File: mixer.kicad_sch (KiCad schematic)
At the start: 22 parts, among them U18 RFFC5072

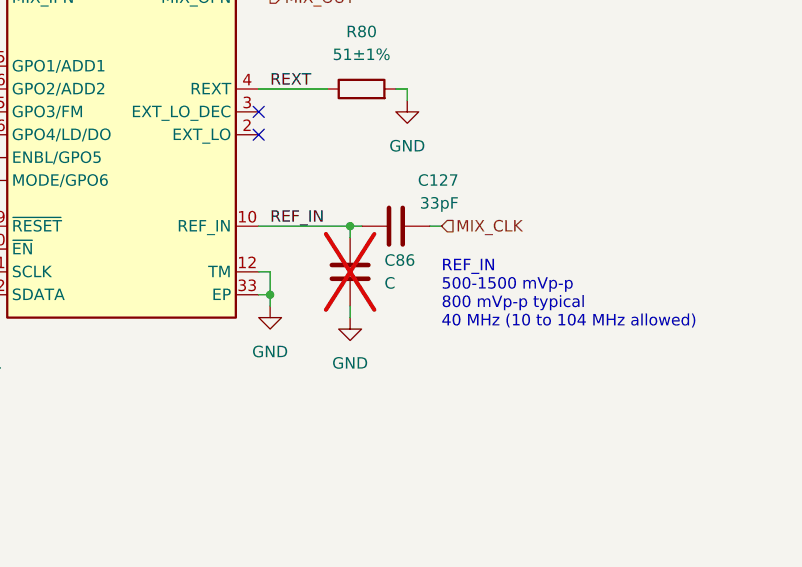
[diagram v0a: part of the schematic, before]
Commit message: update symbol metadata
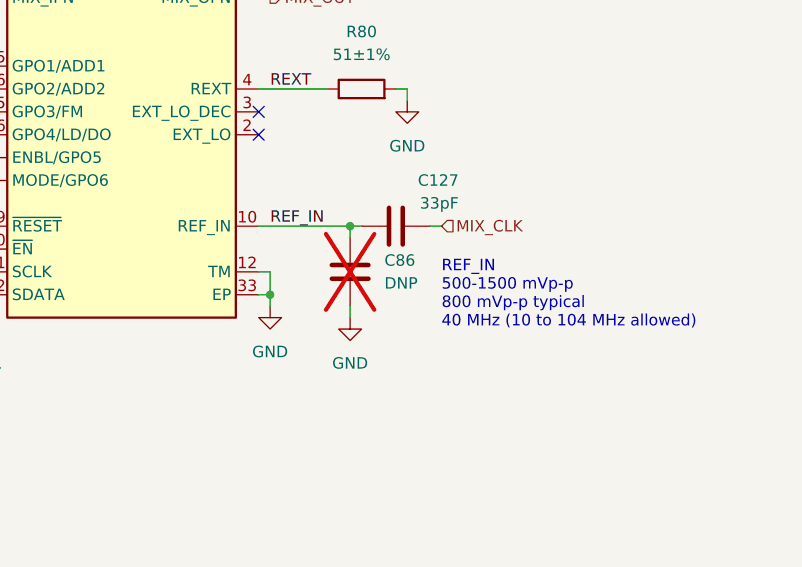
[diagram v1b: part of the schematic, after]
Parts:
- C86: value C -> DNP
- U18: Manufacturer (none) -> Qorvo; Part Number (none) -> RFFC5072TR13; Substitution (none) -> RFFC5072*
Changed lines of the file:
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@@
+      (effects (font (size 1.27 1.27)) hide)
+    )
+    (property "Manufacturer" "Qorvo" (at 156.21 97.79 0)
+      (effects (font (size 1.27 1.27)) hide)
+    )
+    (property "Description" "WIDEBAND SYNTHESIZER/VCO WITH INTEGRATED 6GHz MIXER" (at 156.21 97.79 0)
+      (effects (font (size 1.27 1.27)) hide)
+    )
+    (property "Part Number" "RFFC5072TR13" (at 156.21 97.79 0)
+      (effects (font (size 1.27 1.27)) hide)
+    )
+    (property "Substitution" "RFFC5072*" (at 156.21 97.79 0)
       (effects (font (size 1.27 1.27)) hide)
     )
@@
       (effects (font (size 1.27 1.27)) (justify left))
     )
-    (property "Value" "C" (at 185.42 119.38 0)
-      (effects (font (size 1.27 1.27)) (justify left))
-    )
+    (property "Value" "DNP" (at 185.42 119.38 0)
+      (effects (font (size 1.27 1.27)) (justify left))
+    )

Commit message: Add footprints
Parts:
- C124, C125, C86: footprint (none) -> Capacitor_SMD:C_0201_0603Metric
- R80, R83, R84, R85: footprint (none) -> Resistor_SMD:R_0201_0603Metric
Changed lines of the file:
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@@
       (effects (font (size 1.27 1.27)) (justify left))
     )
-    (property "Footprint" "" (at 216.8652 68.58 0)
+    (property "Footprint" "Capacitor_SMD:C_0201_0603Metric" (at 216.8652 68.58 0)
       (effects (font (size 1.27 1.27)) hide)
     )
@@
       (effects (font (size 1.27 1.27)) (justify left))
     )
-    (property "Footprint" "" (at 209.2452 68.58 0)
+    (property "Footprint" "Capacitor_SMD:C_0201_0603Metric" (at 209.2452 68.58 0)
       (effects (font (size 1.27 1.27)) hide)
     )
@@
       (effects (font (size 1.27 1.27)))
     )
-    (property "Footprint" "" (at 182.88 99.568 90)
+    (property "Footprint" "Resistor_SMD:R_0201_0603Metric" (at 182.88 99.568 90)
       (effects (font (size 1.27 1.27)) hide)
     )
@@
       (effects (font (size 1.27 1.27)))
     )
-    (property "Footprint" "" (at 189.23 61.468 90)
+    (property "Footprint" "Resistor_SMD:R_0201_0603Metric" (at 189.23 61.468 90)
       (effects (font (size 1.27 1.27)) hide)
     )
@@
       (effects (font (size 1.27 1.27)))
     )
-    (property "Footprint" "" (at 199.39 61.468 90)
+    (property "Footprint" "Resistor_SMD:R_0201_0603Metric" (at 199.39 61.468 90)
       (effects (font (size 1.27 1.27)) hide)
     )
@@
       (effects (font (size 1.27 1.27)) (justify right))
     )
-    (property "Footprint" "" (at 217.678 74.93 90)
+    (property "Footprint" "Resistor_SMD:R_0201_0603Metric" (at 217.678 74.93 90)
       (effects (font (size 1.27 1.27)) hide)
     )
@@
       (effects (font (size 1.27 1.27)) (justify left))
     )
-    (property "Footprint" "" (at 182.5752 121.92 0)
-      (effects (font (size 1.27 1.27)) hide)
-    )
+    (property "Footprint" "Capacitor_SMD:C_0201_0603Metric" (at 182.5752 121.92 0)
+      (effects (font (size 1.27 1.27)) hide)
+    )

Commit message: layout wip
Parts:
- C6: footprint Capacitor_SMD:C_0402_1005Metric -> Capacitor_SMD:C_0201_0603Metric; Manufacturer Samsung -> Murata; Part Number CL05C331JB5NNNC -> GRM0335C1E331JA01D; Substitution any equivalent -> GRM0335C1E331JA01*
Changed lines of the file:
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@@
       (effects (font (size 1.27 1.27)) (justify left))
     )
-    (property "Footprint" "Capacitor_SMD:C_0402_1005Metric" (at 185.1152 68.58 0)
+    (property "Footprint" "Capacitor_SMD:C_0201_0603Metric" (at 185.1152 68.58 0)
       (effects (font (size 1.27 1.27)) hide)
     )
@@
       (effects (font (size 1.27 1.27)) hide)
     )
-    (property "Part Number" "CL05C331JB5NNNC" (at 184.15 64.77 0)
-      (effects (font (size 1.27 1.27)) hide)
-    )
-    (property "Substitution" "any equivalent" (at 184.15 64.77 0)
-      (effects (font (size 1.27 1.27)) hide)
-    )
-    (property "Description" "CAP CER 330PF 50V C0G/NP0 0402" (at 184.15 64.77 0)
-      (effects (font (size 1.27 1.27)) hide)
-    )
-    (property "Manufacturer" "Samsung" (at 184.15 64.77 0)
+    (property "Part Number" "GRM0335C1E331JA01D" (at 184.15 64.77 0)
+      (effects (font (size 1.27 1.27)) hide)
+    )
+    (property "Substitution" "GRM0335C1E331JA01*" (at 184.15 64.77 0)
+      (effects (font (size 1.27 1.27)) hide)
+    )
+    (property "Description" "CAP CER 330PF 25V C0G/NP0 0201" (at 184.15 64.77 0)
+      (effects (font (size 1.27 1.27)) hide)
+    )
+    (property "Manufacturer" "Murata" (at 184.15 64.77 0)
       (effects (font (size 1.27 1.27)) hide)
     )
@@
       (effects (font (size 1.27 1.27)) (justify left))
     )
-    (property "Footprint" "Capacitor_SMD:C_0402_1005Metric" (at 195.2752 68.58 0)
+    (property "Footprint" "Capacitor_SMD:C_0201_0603Metric" (at 195.2752 68.58 0)
       (effects (font (size 1.27 1.27)) hide)
     )
@@
       (effects (font (size 1.27 1.27)) hide)
     )
-    (property "Part Number" "CL05C331JB5NNNC" (at 194.31 64.77 0)
-      (effects (font (size 1.27 1.27)) hide)
-    )
-    (property "Substitution" "any equivalent" (at 194.31 64.77 0)
-      (effects (font (size 1.27 1.27)) hide)
-    )
-    (property "Description" "CAP CER 330PF 50V C0G/NP0 0402" (at 194.31 64.77 0)
-      (effects (font (size 1.27 1.27)) hide)
-    )
-    (property "Manufacturer" "Samsung" (at 194.31 64.77 0)
-      (effects (font (size 1.27 1.27)) hide)
-    )
+    (property "Part Number" "GRM0335C1E331JA01D" (at 194.31 64.77 0)
+      (effects (font (size 1.27 1.27)) hide)
+    )
+    (property "Substitution" "GRM0335C1E331JA01*" (at 194.31 64.77 0)
+      (effects (font (size 1.27 1.27)) hide)
+    )
+    (property "Description" "CAP CER 330PF 25V C0G/NP0 0201" (at 194.31 64.77 0)
+      (effects (font (size 1.27 1.27)) hide)
+    )
+    (property "Manufacturer" "Murata" (at 194.31 64.77 0)
+      (effects (font (size 1.27 1.27)) hide)
+    )

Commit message: passive component selections
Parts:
- C124: Manufacturer (none) -> Murata; Part Number (none) -> GRM0335C1H8R2BA01D; Substitution (none) -> GRM0335C1H8R2BA01*
- C125: Manufacturer (none) -> Murata; Part Number (none) -> GRM0335C1H181JA01D; Substitution (none) -> GRM0335C1H181JA01*
- R80: Manufacturer (none) -> Yageo; Part Number (none) -> RC0201FR-0751KL; Substitution (none) -> any equivalent
- R83, R84: Manufacturer (none) -> Yageo; Part Number (none) -> RC0201JR-07470RL; Substitution (none) -> any equivalent
- R85: Manufacturer (none) -> Yageo; Part Number (none) -> RC0201JR-0722KL; Substitution (none) -> any equivalent
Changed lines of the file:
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@@
+      (effects (font (size 1.27 1.27)) hide)
+    )
+    (property "Description" "CAP CER 180PF 50V C0G/NP0 0201" (at 215.9 64.77 0)
+      (effects (font (size 1.27 1.27)) hide)
+    )
+    (property "Manufacturer" "Murata" (at 215.9 64.77 0)
+      (effects (font (size 1.27 1.27)) hide)
+    )
+    (property "Part Number" "GRM0335C1H181JA01D" (at 215.9 64.77 0)
+      (effects (font (size 1.27 1.27)) hide)
+    )
+    (property "Substitution" "GRM0335C1H181JA01*" (at 215.9 64.77 0)
       (effects (font (size 1.27 1.27)) hide)
     )
@@
       (effects (font (size 1.27 1.27)) hide)
     )
+    (property "Description" "CAP CER 8.2PF 50V C0G/NP0 0201" (at 208.28 64.77 0)
+      (effects (font (size 1.27 1.27)) hide)
+    )
+    (property "Manufacturer" "Murata" (at 208.28 64.77 0)
+      (effects (font (size 1.27 1.27)) hide)
+    )
+    (property "Part Number" "GRM0335C1H8R2BA01D" (at 208.28 64.77 0)
+      (effects (font (size 1.27 1.27)) hide)
+    )
+    (property "Substitution" "GRM0335C1H8R2BA01*" (at 208.28 64.77 0)
+      (effects (font (size 1.27 1.27)) hide)
+    )
     (pin "2")
     (pin "1")
@@
     )
     (property "Datasheet" "~" (at 182.88 97.79 0)
+      (effects (font (size 1.27 1.27)) hide)
+    )
+    (property "Description" "RES 51K OHM 1% 1/20W 0201" (at 182.88 97.79 0)
+      (effects (font (size 1.27 1.27)) hide)
+    )
+    (property "Manufacturer" "Yageo" (at 182.88 97.79 0)
+      (effects (font (size 1.27 1.27)) hide)
+    )
+    (property "Part Number" "RC0201FR-0751KL" (at 182.88 97.79 0)
+      (effects (font (size 1.27 1.27)) hide)
+    )
+    (property "Substitution" "any equivalent" (at 182.88 97.79 0)
       (effects (font (size 1.27 1.27)) hide)
     )
@@
       (effects (font (size 1.27 1.27)) hide)
     )
+    (property "Description" "RES 470 OHM 5% 1/20W 0201" (at 189.23 59.69 0)
+      (effects (font (size 1.27 1.27)) hide)
+    )
+    (property "Manufacturer" "Yageo" (at 189.23 59.69 0)
+      (effects (font (size 1.27 1.27)) hide)
+    )
+    (property "Part Number" "RC0201JR-07470RL" (at 189.23 59.69 0)
+      (effects (font (size 1.27 1.27)) hide)
+    )
+    (property "Substitution" "any equivalent" (at 189.23 59.69 0)
+      (effects (font (size 1.27 1.27)) hide)
+    )
     (pin "2")
     (pin "1")
@@
       (effects (font (size 1.27 1.27)) hide)
     )
+    (property "Description" "RES 470 OHM 5% 1/20W 0201" (at 199.39 59.69 0)
+      (effects (font (size 1.27 1.27)) hide)
+    )
+    (property "Manufacturer" "Yageo" (at 199.39 59.69 0)
+      (effects (font (size 1.27 1.27)) hide)
+    )
+    (property "Part Number" "RC0201JR-07470RL" (at 199.39 59.69 0)
+      (effects (font (size 1.27 1.27)) hide)
+    )
+    (property "Substitution" "any equivalent" (at 199.39 59.69 0)
+      (effects (font (size 1.27 1.27)) hide)
+    )
     (pin "2")
     (pin "1")
@@
       (effects (font (size 1.27 1.27)) hide)
     )
+    (property "Description" "RES 22K OHM 5% 1/20W 0201" (at 215.9 74.93 0)
+      (effects (font (size 1.27 1.27)) hide)
+    )
+    (property "Manufacturer" "Yageo" (at 215.9 74.93 0)
+      (effects (font (size 1.27 1.27)) hide)
+    )
+    (property "Part Number" "RC0201JR-0722KL" (at 215.9 74.93 0)
+      (effects (font (size 1.27 1.27)) hide)
+    )
+    (property "Substitution" "any equivalent" (at 215.9 74.93 0)
+      (effects (font (size 1.27 1.27)) hide)
+    )
